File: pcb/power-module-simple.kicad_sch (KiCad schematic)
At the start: 37 parts, among them J1 USB_C_PowerOnly_6P, J2 Power, U1 AZ1084-3.3, U2 LM66200DRLR

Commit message: Attribute updates; generated production files
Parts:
- R3: footprint Resistor_SMD:R_0805_2012Metric -> Resistor_SMD:R_0603_1608Metric; Digikey RMCF0805FT10K0CT-ND -> 541-3993-2-ND; JLCPCB C17673 -> (none); LCSC C17673 -> C2907166; MN (none) -> FOJAN; MPN (none) -> FRC0603J472 TS; Mouser 71-CRCW080510K0FKEAC -> 71-CRCW06034K70JNEAC
- R4: footprint Resistor_SMD:R_0805_2012Metric -> Resistor_SMD:R_0603_1608Metric; Digikey RMCF0805FT10K0CT-ND -> 541-1.00KHTR-ND; JLCPCB C17513 -> (none); LCSC C17513 -> C2907113; MN (none) -> Vishay; MPN (none) -> CRCW06031K00FKEA; Mouser 71-CRCW080510K0FKEAC -> 71-CRCW0603-1.0K-E3
- S1: now left out of the parts list
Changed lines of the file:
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@@
 			)
 		)
-		(property "Footprint" "Resistor_SMD:R_0805_2012Metric"
+		(property "Footprint" "Resistor_SMD:R_0603_1608Metric"
 			(at 147.32 177.8 0)
 			(effects
@@
 			)
 		)
-		(property "Datasheet" ""
+		(property "Datasheet" "https://www.vishay.com/docs/28773/crcwce3.pdf"
 			(at 147.32 177.8 0)
 			(effects
@@
 			)
 		)
-		(property "Description" ""
+		(property "Description" "Thick Film Resistors - SMD 1/10Watt 4.7Kohms 5% Commercial Use"
 			(at 147.32 177.8 0)
 			(effects
@@
 			)
 		)
-		(property "Digikey" "RMCF0805FT10K0CT-ND"
+		(property "MN" "FOJAN"
 			(at 147.32 177.8 0)
 			(effects
 				(font
-					(size 1 1)
-					(color 223 129 255 1)
+					(size 1.27 1.27)
 				)
 				(hide yes)
 			)
 		)
-		(property "JLCPCB" "C17673"
+		(property "MPN" "FRC0603J472 TS"
 			(at 147.32 177.8 0)
 			(effects
 				(font
-					(size 1 1)
-					(color 223 129 255 1)
+					(size 1.27 1.27)
 				)
 				(hide yes)
 			)
 		)
-		(property "LCSC" "C17673"
+		(property "Mouser" "71-CRCW06034K70JNEAC"
 			(at 147.32 177.8 0)
 			(effects
@@
 			)
 		)
-		(property "Mouser" "71-CRCW080510K0FKEAC"
+		(property "Digikey" "541-3993-2-ND"
 			(at 147.32 177.8 0)
 			(effects
@@
 			)
 		)
-		(property "Notes" ""
+		(property "LCSC" "C2907166"
 			(at 147.32 177.8 0)
 			(effects
@@
 			)
 		)
-		(property "Height" ""
-			(at 147.32 177.8 0)
-			(effects
-				(font
-					(size 1.27 1.27)
-				)
-			)
-		)
-		(property "LCSC_MF_PN" ""
-			(at 147.32 177.8 0)
-			(effects
-				(font
-					(size 1.27 1.27)
-				)
-			)
-		)
-		(property "MN_PN" ""
-			(at 147.32 177.8 0)
-			(effects
-				(font
-					(size 1.27 1.27)
-				)
-			)
-		)
-		(property "Mouser Part Number" ""
-			(at 147.32 177.8 0)
-			(effects
-				(font
-					(size 1.27 1.27)
-				)
-			)
-		)
-		(property "Mouser Price/Stock" ""
-			(at 147.32 177.8 0)
-			(effects
-				(font
-					(size 1.27 1.27)
-				)
-			)
-		)
 		(pin "1"
 		)
@@
 		(unit 1)
 		(exclude_from_sim no)
-		(in_bom yes)
+		(in_bom no)
 		(on_board yes)
 		(dnp no)
@@
 			)
 		)
-		(property "Height" ""
-			(at 124.46 45.72 0)
-			(effects
-				(font
-					(size 1.27 1.27)
-				)
-			)
-		)
-		(property "LCSC_MF_PN" ""
-			(at 124.46 45.72 0)
-			(effects
-				(font
-					(size 1.27 1.27)
-				)
-			)
-		)
-		(property "MN_PN" ""
-			(at 124.46 45.72 0)
-			(effects
-				(font
-					(size 1.27 1.27)
-				)
-			)
-		)
-		(property "Mouser Part Number" ""
-			(at 124.46 45.72 0)
-			(effects
-				(font
-					(size 1.27 1.27)
-				)
-			)
-		)
-		(property "Mouser Price/Stock" ""
-			(at 124.46 45.72 0)
-			(effects
-				(font
-					(size 1.27 1.27)
-				)
-			)
-		)
 		(pin "2"
 		)
@@
 			)
 		)
-		(property "Footprint" "Resistor_SMD:R_0805_2012Metric"
+		(property "Footprint" "Resistor_SMD:R_0603_1608Metric"
 			(at 163.83 177.8 0)
 			(effects
@@
 			)
 		)
-		(property "Datasheet" ""
+		(property "Datasheet" "https://www.vishay.com/docs/20035/dcrcwe3.pdf"
 			(at 163.83 177.8 0)
 			(effects
@@
 			)
 		)
-		(property "Description" ""
+		(property "Description" "Thick Film Resistors - SMD 1/10watt 1.0Kohms 1%"
 			(at 163.83 177.8 0)
 			(effects
@@
 			)
 		)
-		(property "Digikey" "RMCF0805FT10K0CT-ND"
+		(property "MN" "Vishay"
 			(at 163.83 177.8 0)
 			(effects
 				(font
-					(size 1 1)
-					(color 223 129 255 1)
+					(size 1.27 1.27)
 				)
 				(hide yes)
 			)
 		)
-		(property "JLCPCB" "C17513"
+		(property "MPN" "CRCW06031K00FKEA"
 			(at 163.83 177.8 0)
 			(effects
 				(font
-					(size 1 1)
-					(color 223 129 255 1)
+					(size 1.27 1.27)
 				)
 				(hide yes)
 			)
 		)
-		(property "LCSC" "C17513"
+		(property "Mouser" "71-CRCW0603-1.0K-E3"
 			(at 163.83 177.8 0)
 			(effects
@@
 			)
 		)
-		(property "Mouser" "71-CRCW080510K0FKEAC"
+		(property "Digikey" "541-1.00KHTR-ND"
 			(at 163.83 177.8 0)
 			(effects
@@
 			)
 		)
-		(property "Notes" ""
+		(property "LCSC" "C2907113"
 			(at 163.83 177.8 0)
 			(effects
@@
 			)
 		)
-		(property "Height" ""
-			(at 163.83 177.8 0)
-			(effects
-				(font
-					(size 1.27 1.27)
-				)
-			)
-		)
-		(property "LCSC_MF_PN" ""
-			(at 163.83 177.8 0)
-			(effects
-				(font
-					(size 1.27 1.27)
-				)
-			)
-		)
-		(property "MN_PN" ""
-			(at 163.83 177.8 0)
-			(effects
-				(font
-					(size 1.27 1.27)
-				)
-			)
-		)
-		(property "Mouser Part Number" ""
-			(at 163.83 177.8 0)
-			(effects
-				(font
-					(size 1.27 1.27)
-				)
-			)
-		)
-		(property "Mouser Price/Stock" ""
-			(at 163.83 177.8 0)
-			(effects
-				(font
-					(size 1.27 1.27)
-				)
-			)
-		)
 		(pin "1"
 		)
@@
 			)
 		)
-		(property "Height" ""
-			(at 133.35 45.72 0)
-			(effects
-				(font
-					(size 1.27 1.27)
-				)
-			)
-		)
-		(property "LCSC_MF_PN" ""
-			(at 133.35 45.72 0)
-			(effects
-				(font
-					(size 1.27 1.27)
-				)
-			)
-		)
-		(property "MN_PN" ""
-			(at 133.35 45.72 0)
-			(effects
-				(font
-					(size 1.27 1.27)
-				)
-			)
-		)
-		(property "Mouser Part Number" ""
-			(at 133.35 45.72 0)
-			(effects
-				(font
-					(size 1.27 1.27)
-				)
-			)
-		)
-		(property "Mouser Price/Stock" ""
-			(at 133.35 45.72 0)
-			(effects
-				(font
-					(size 1.27 1.27)
-				)
-			)
-		)

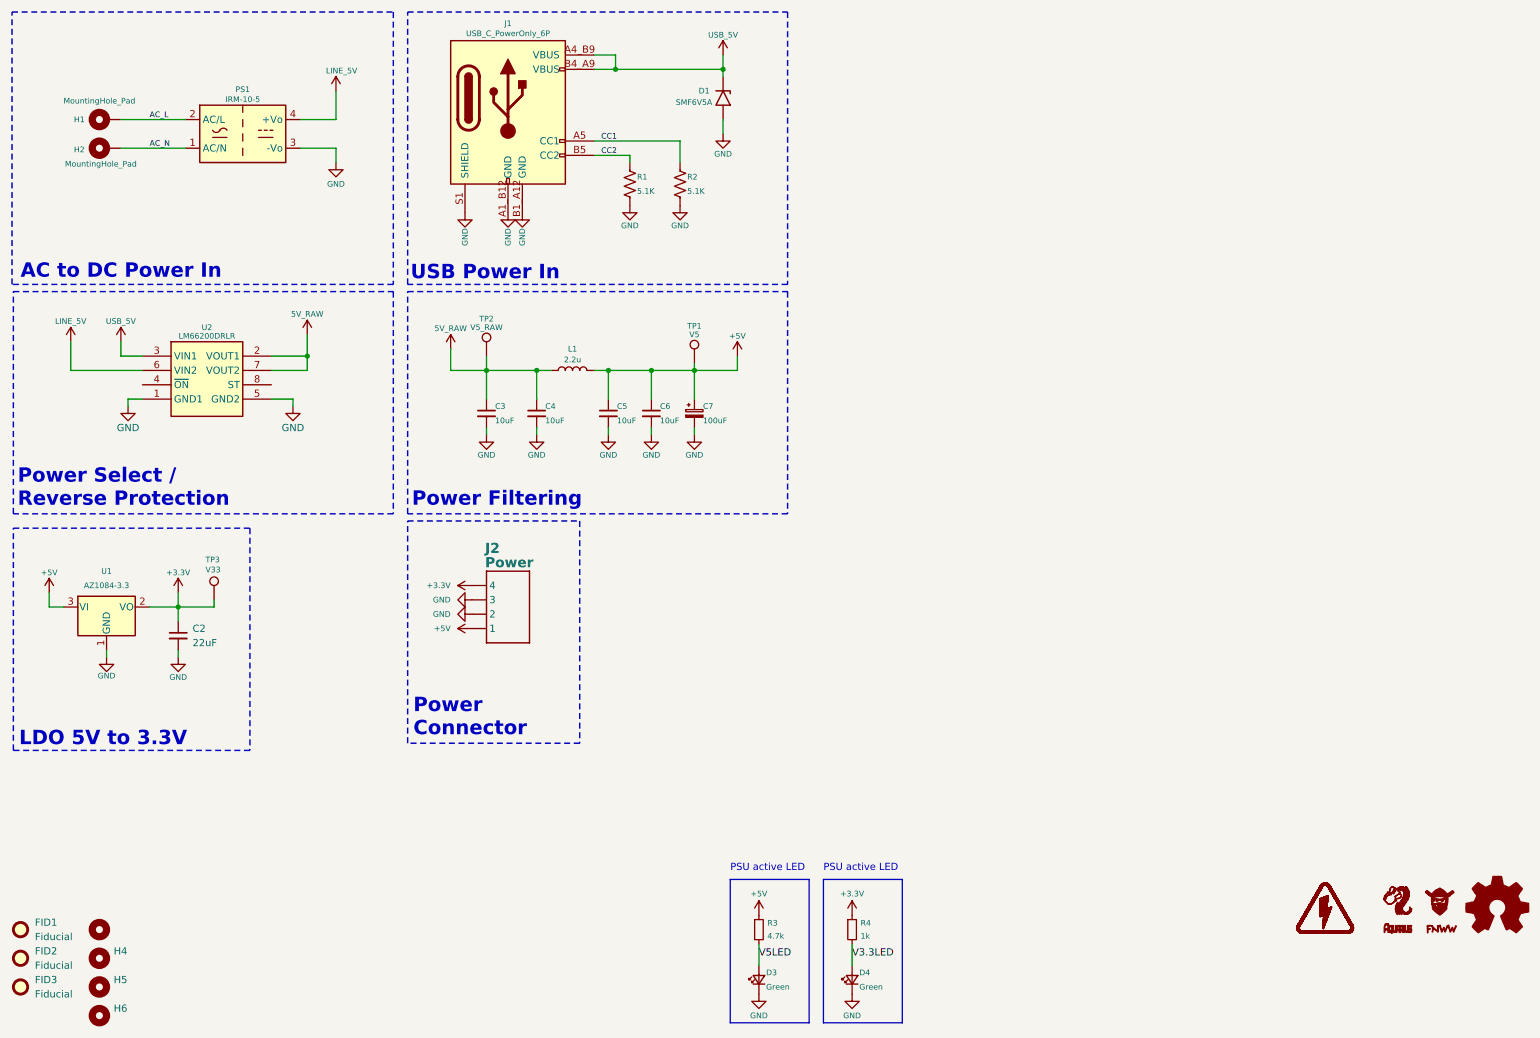
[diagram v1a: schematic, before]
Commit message: Updated silkscreen and LED size
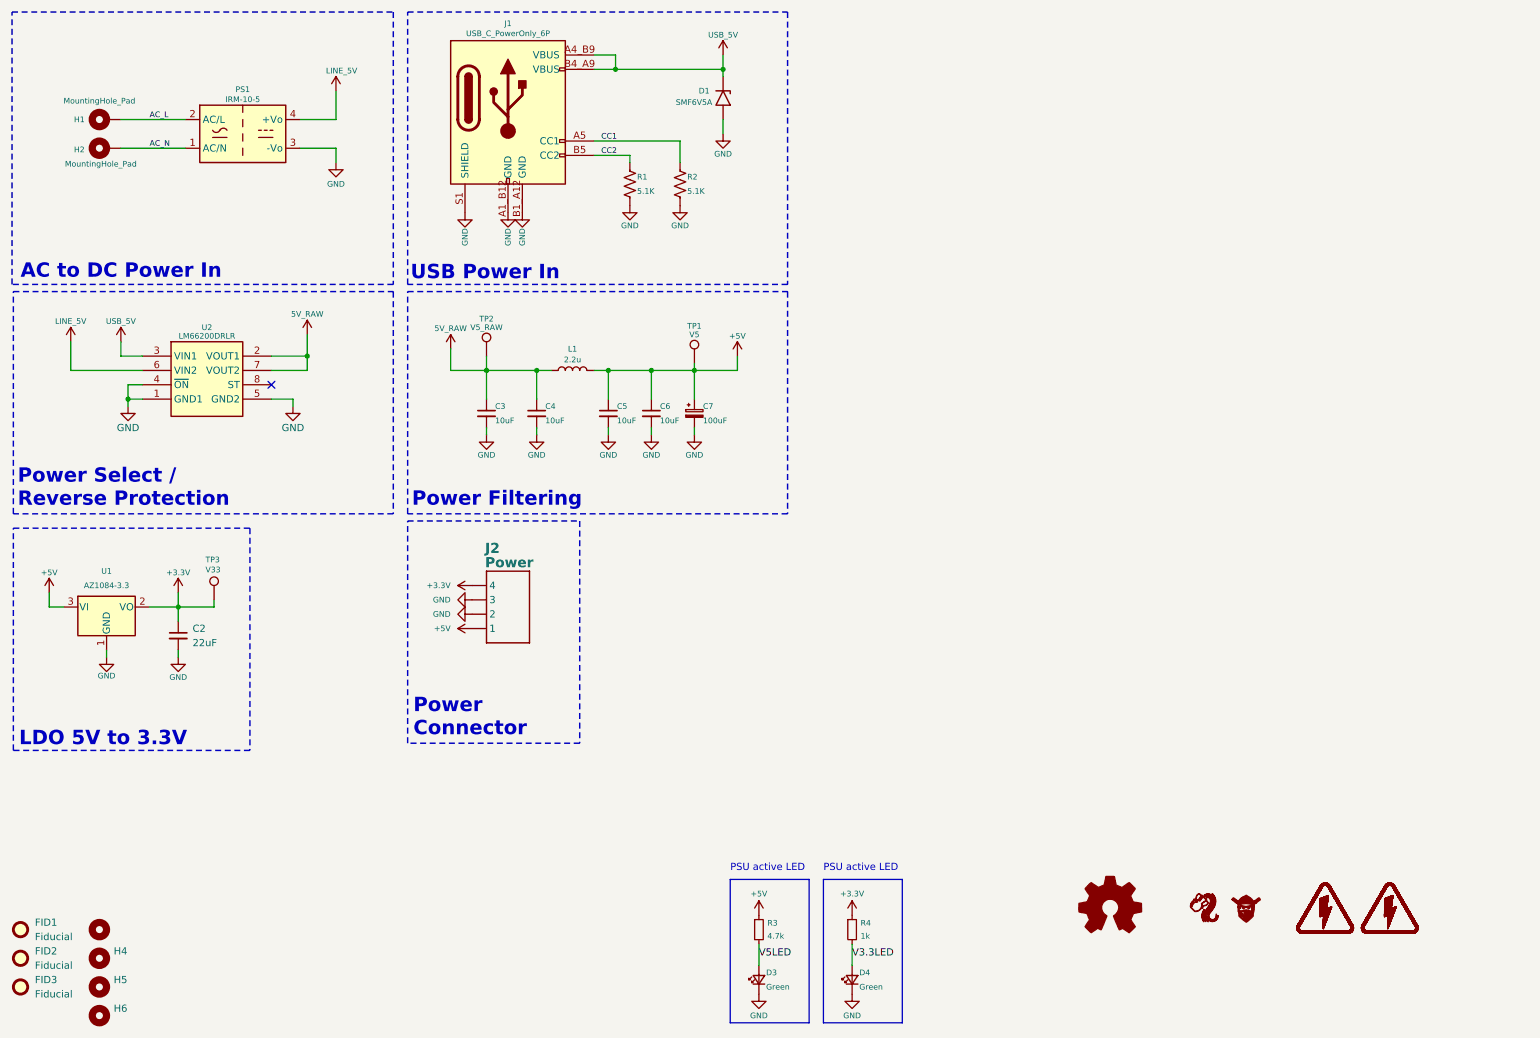
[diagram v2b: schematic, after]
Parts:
- removed LOGO1: Logo_Open_Hardware_Small, Symbol:OSHW-Symbol_6.7x6mm_SilkScreen, symbol Graphic:Logo_Open_Hardware_Small
- removed LOGO2: ~, CRGM Logos:Aquarius Logo 5mm, symbol CRGM Logos:Aquarius Logo
- removed LOGO3: ~, CRGM Logos:FNWW Face 5mm, symbol CRGM Logos:FNWW Face
- removed LOGO4: ~, CRGM Logos:FNWW Name 2mmx5mm, symbol CRGM Logos:FNWW Name
- removed LOGO5: ~, CRGM Logos:Aquarius Name 2mmx5mm, symbol CRGM Logos:Aquarius Name
- added LOGO1: ~, CRGM Logos:FNWW Face 10mm, symbol CRGM Logos:FNWW Face
- added LOGO2: Logo_Open_Hardware_Small, Symbol:OSHW-Logo_5.7x6mm_SilkScreen, symbol Graphic:Logo_Open_Hardware_Small
- added LOGO3: ~, CRGM Logos:Aquarius Logo 10mm, symbol CRGM Logos:Aquarius Logo
- added S2: ~, CRGM Symbols:HIGH-VOLTAGE-5MM, symbol CRGM Symbols:High Voltage
- D3, D4: footprint LED_SMD:LED_0805_2012Metric -> LED_SMD:LED_0603_1608Metric; Digikey (none) -> 160-1446-2-ND; LCSC C965815 -> C965804; MN (none) -> XINGLIGHT; MPN (none) -> XL-1608UGC-04; Mouser (none) -> 859-LTST-C191KGKT; Notes 20mA -> (none)
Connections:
- net GND: now also U2.4 (~{ON})
- no-connect marks 0 -> 1

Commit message: Changed switching mechanism; updated power delivery for v3.3
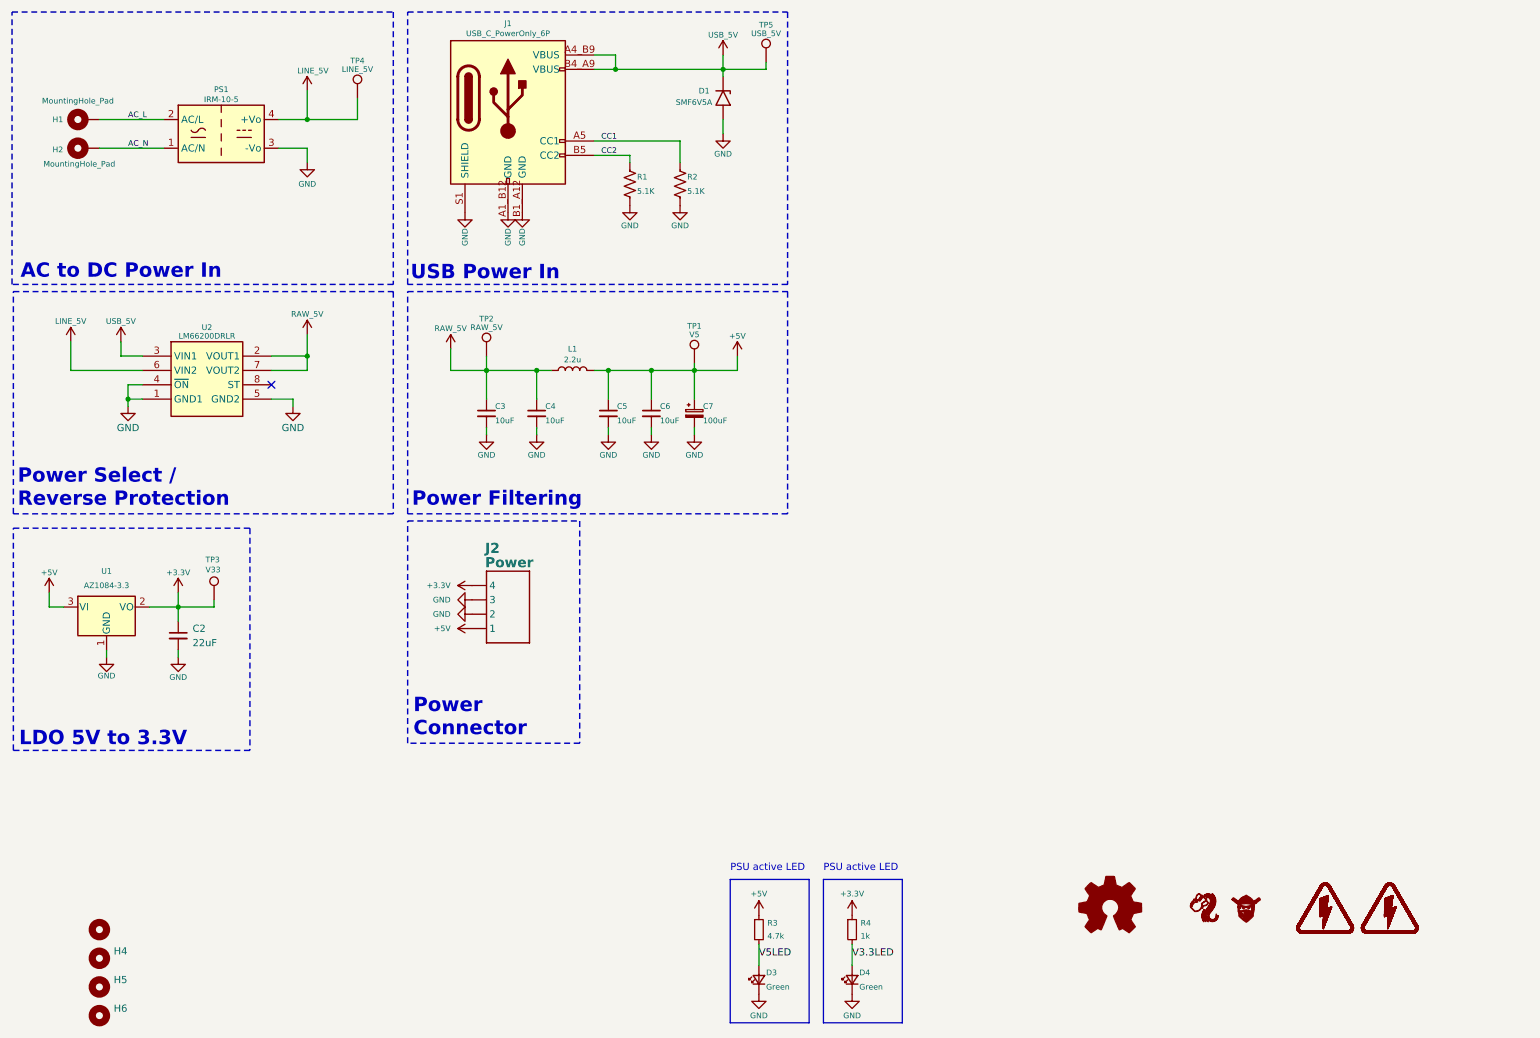
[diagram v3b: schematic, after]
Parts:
- removed FID1, FID2, FID3: Fiducial, Fiducial:Fiducial_0.75mm_Mask1.5mm, symbol Mechanical:Fiducial
- added TP4: LINE_5V, TestPoint:TestPoint_Pad_D1.0mm, symbol Connector:TestPoint
- added TP5: USB_5V, TestPoint:TestPoint_Pad_D1.0mm, symbol Connector:TestPoint
- TP2: value V5_RAW -> RAW_5V
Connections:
- net LINE_5V: now also TP4.1
- net USB_5V: now also TP5.1
- net 5V_RAW renamed RAW_5V
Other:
- moved on the sheet: H1, H2, PS1

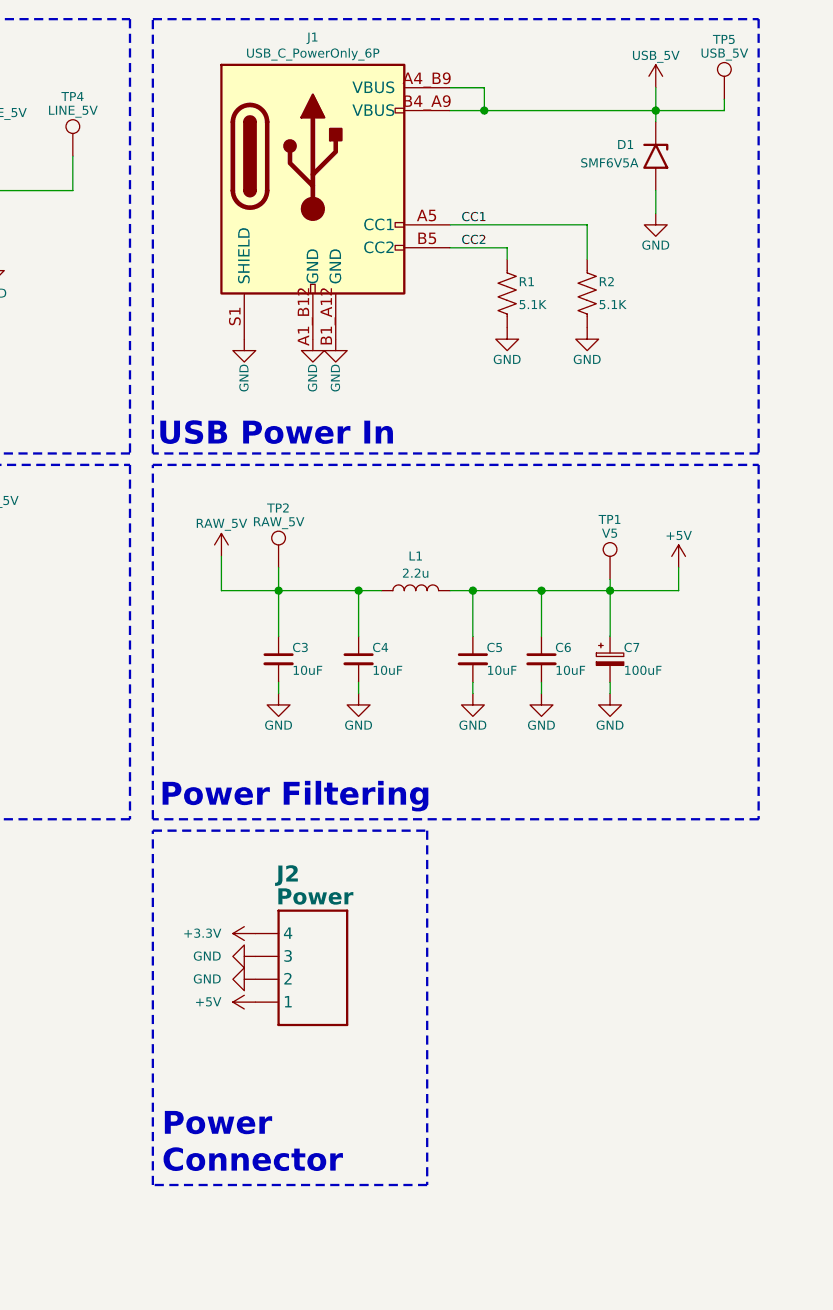
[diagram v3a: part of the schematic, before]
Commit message: Fixed AZ1084 footprint
Fixed USB-C Connector / symbol mismatch
Moved parts around
Moved USB-C connector from overhanging.
Generated ibom.
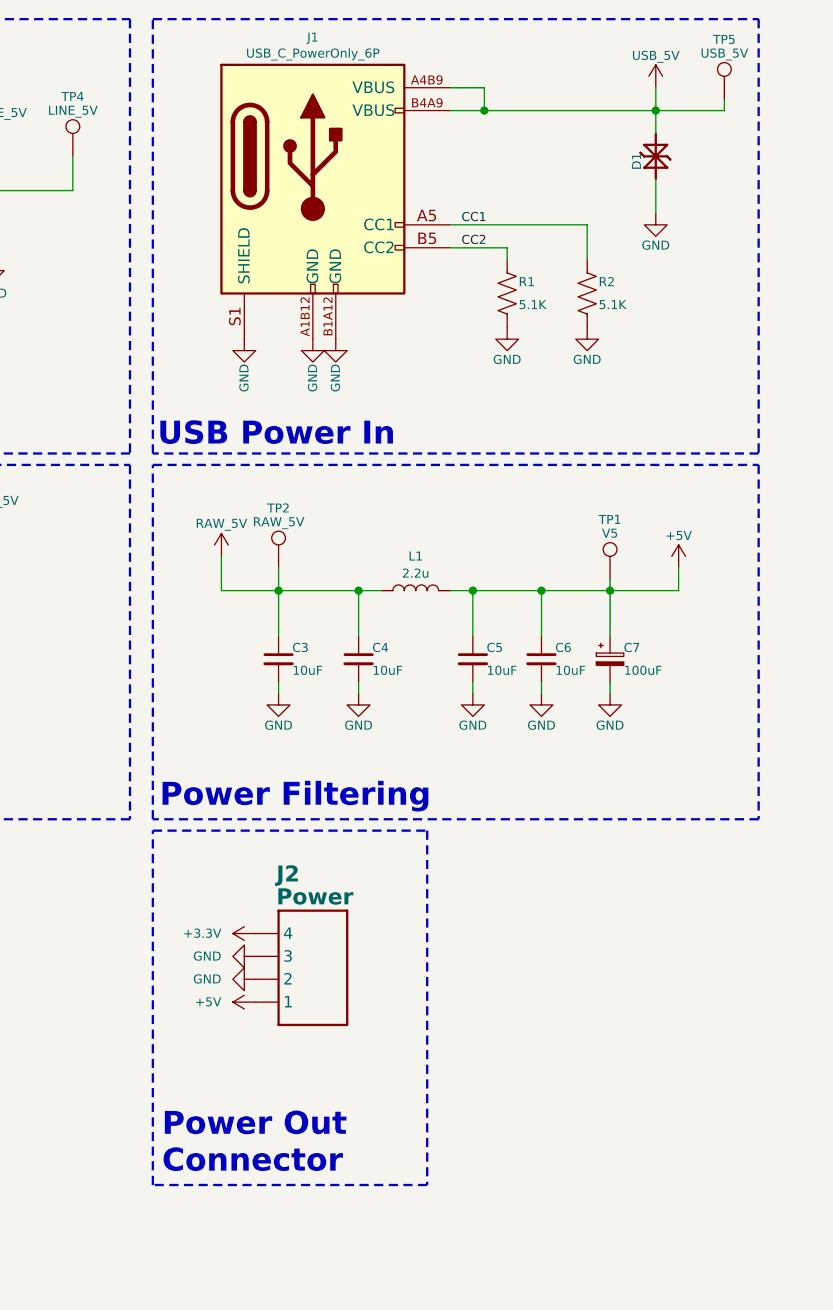
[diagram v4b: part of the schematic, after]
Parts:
- removed D1: SMF6V5A, Diode_SMD:D_SOD-123F, symbol Diode:SMF6V5A
- added D1: PESD5V5C1BL, CRGM Passive:DFN1006-2, symbol CRGM Passive:PESD5V5C1BLYL
- U1: footprint Package_TO_SOT_SMD:TO-252-2 -> CRGM Power:TO-252-2
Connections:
- net GND: now also J1.A1B12 (GND), J1.B1A12 (GND), D1.1 (K1); no longer J1.A1_B12 (GND), J1.B1_A12 (GND)
- net USB_5V: now also J1.A4B9 (VBUS), J1.B4A9 (VBUS), D1.2 (K2); no longer J1.A4_B9 (VBUS), J1.B4_A9 (VBUS)
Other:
- note added: "Power Out Connector"
- note removed: "Power Connector"
